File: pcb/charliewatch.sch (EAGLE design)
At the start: 85 parts, among them U2 CC430F5137IRGZR, X1 CRYSTALS-NOGND-IQXC-25, X2 FA-128

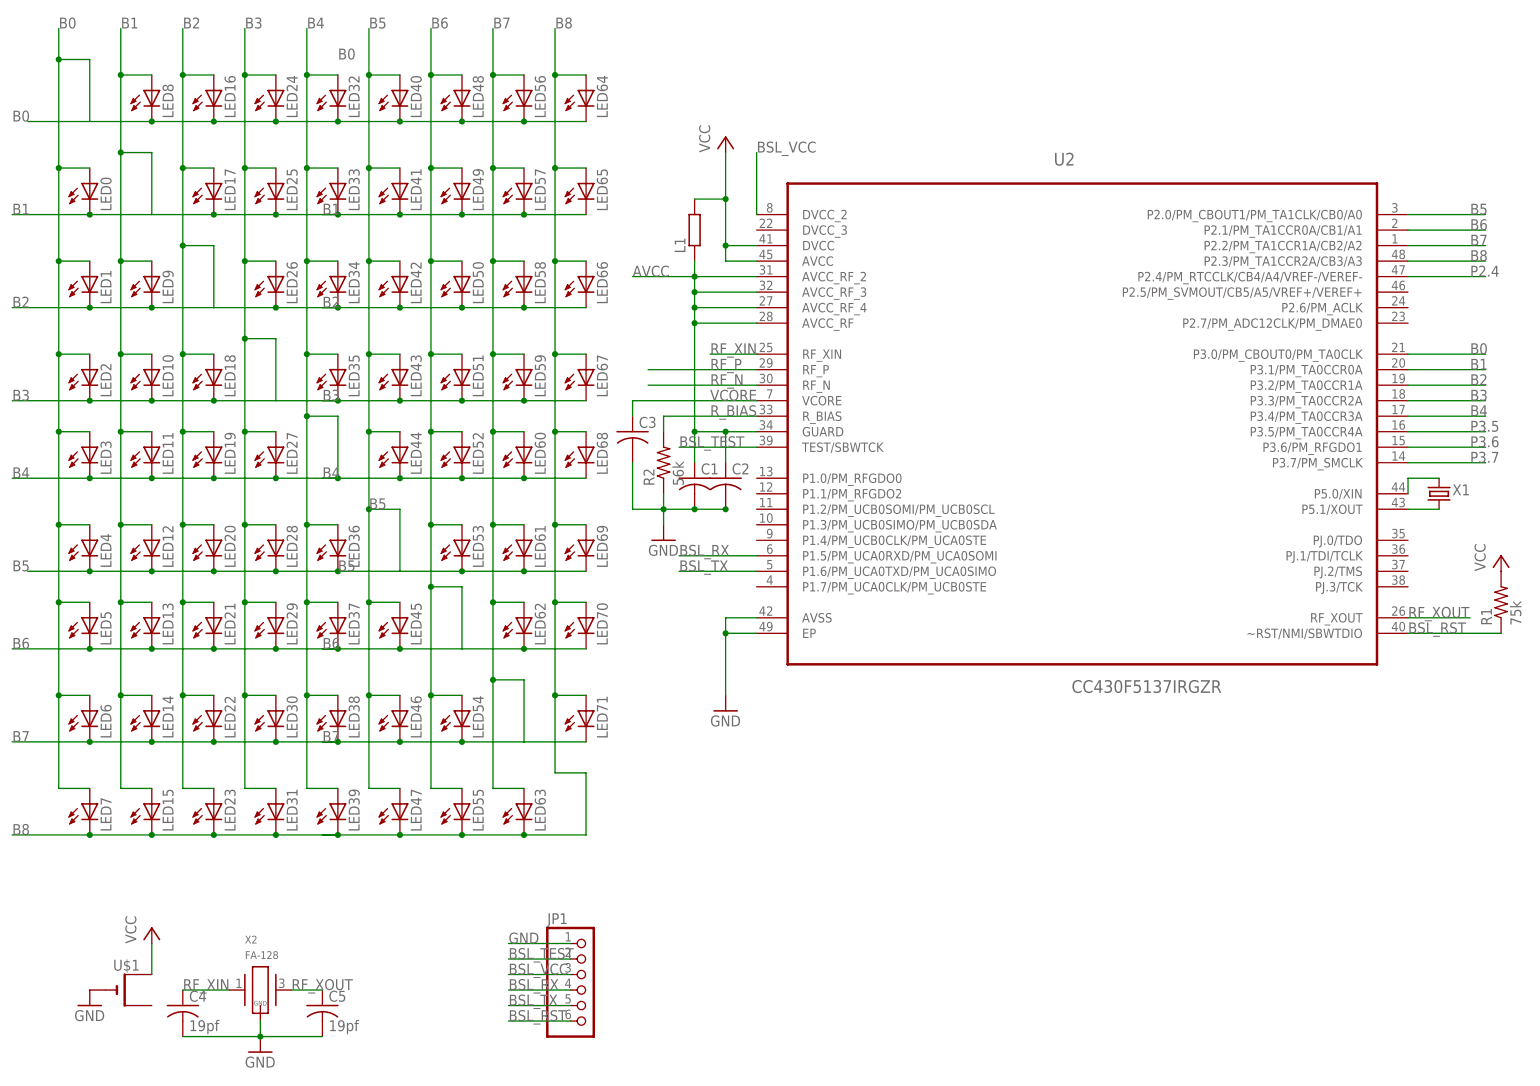
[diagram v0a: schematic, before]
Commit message: fixed drc errors, one missing vcc pin
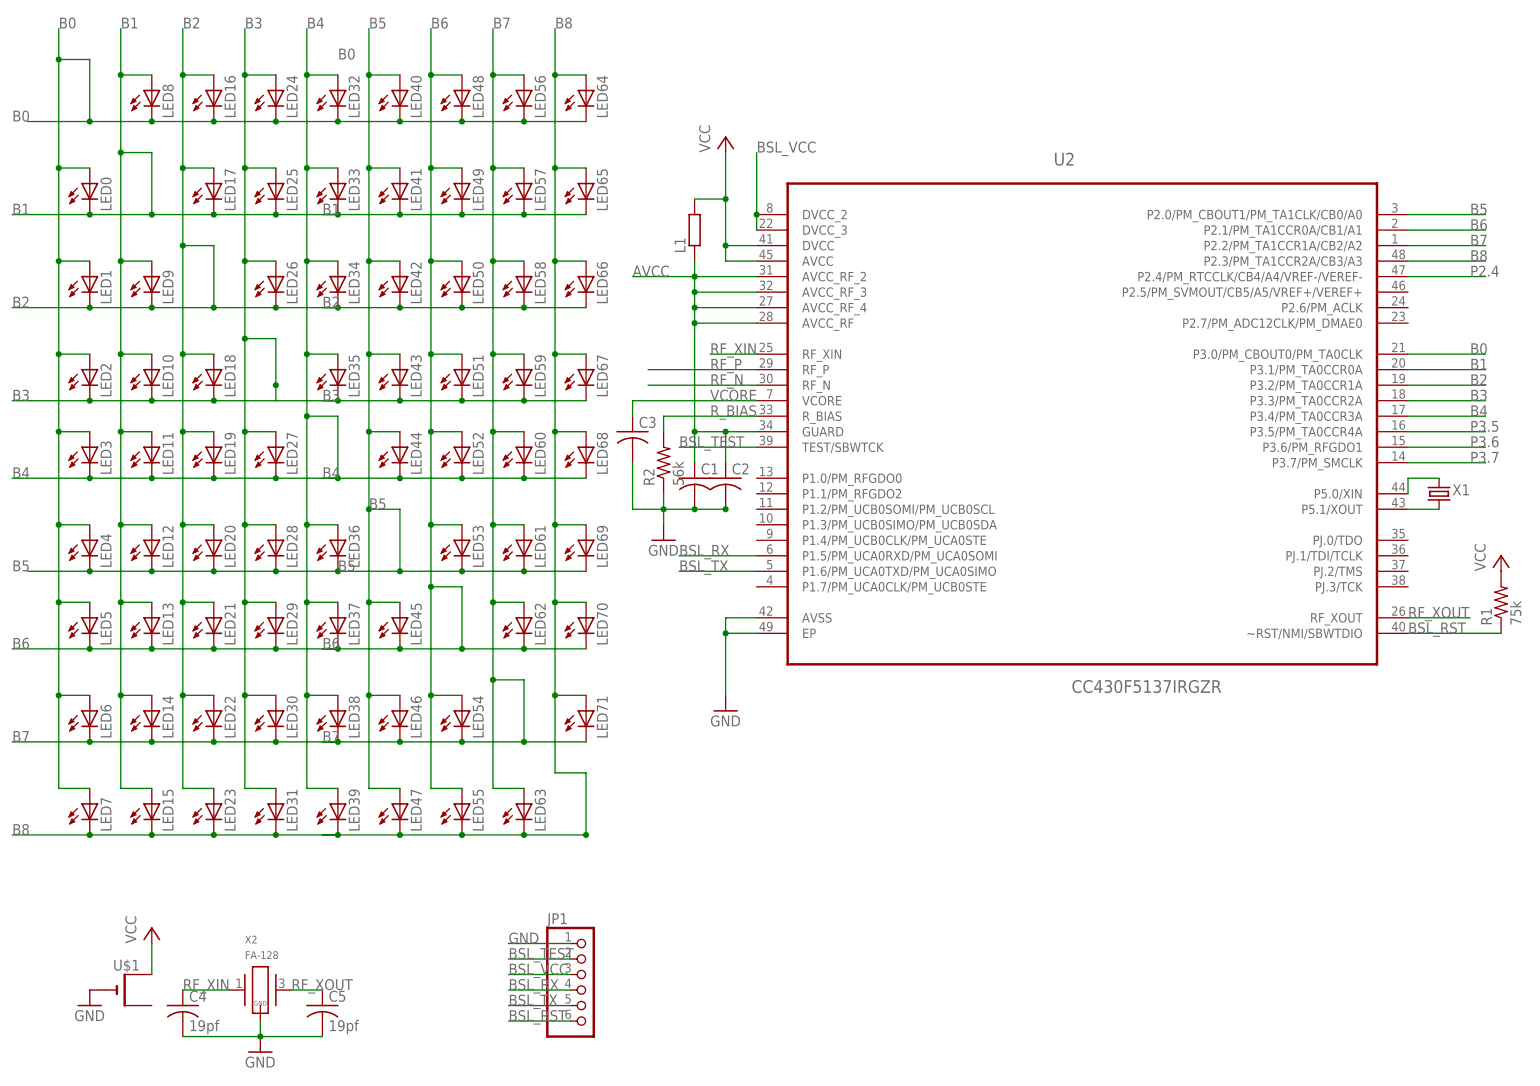
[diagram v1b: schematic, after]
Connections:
- net BSL_VCC: now also U2.DVCC_3
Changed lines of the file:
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@@
 <pinref part="LED67" gate="G$1" pin="C"/>
 <junction x="55.88" y="119.38"/>
-<wire x1="45.72" y1="129.54" x2="45.72" y2="119.38" width="0.1524" layer="91"/>
+<wire x1="45.72" y1="129.54" x2="45.72" y2="121.92" width="0.1524" layer="91"/>
+<junction x="45.72" y="121.92"/>
+<wire x1="45.72" y1="121.92" x2="45.72" y2="119.38" width="0.1524" layer="91"/>
 </segment>
 <segment>
@@
 <junction x="55.88" y="134.62"/>
 <wire x1="35.56" y1="144.78" x2="35.56" y2="134.62" width="0.1524" layer="91"/>
+<junction x="35.56" y="134.62"/>
 </segment>
 <segment>
@@
 <junction x="55.88" y="149.86"/>
 <wire x1="25.4" y1="160.02" x2="25.4" y2="149.86" width="0.1524" layer="91"/>
+<junction x="25.4" y="149.86"/>
 </segment>
 <segment>
@@
 <junction x="55.88" y="165.1"/>
 <wire x1="15.24" y1="175.26" x2="15.24" y2="165.1" width="0.1524" layer="91"/>
+<junction x="15.24" y="165.1"/>
 </segment>
 <segment>
@@
 <junction x="91.44" y="99.06"/>
 <wire x1="96.52" y1="48.26" x2="96.52" y2="58.42" width="0.1524" layer="91"/>
+<junction x="96.52" y="48.26"/>
 </segment>
 <segment>
@@
 <junction x="55.88" y="63.5"/>
 <wire x1="86.36" y1="73.66" x2="86.36" y2="63.5" width="0.1524" layer="91"/>
+<junction x="86.36" y="63.5"/>
 </segment>
 <segment>
@@
 <junction x="55.88" y="78.74"/>
 <wire x1="76.2" y1="88.9" x2="76.2" y2="78.74" width="0.1524" layer="91"/>
+<junction x="76.2" y="78.74"/>
 </segment>
 <segment>
@@
 <junction x="55.88" y="91.44"/>
 <wire x1="66.04" y1="101.6" x2="66.04" y2="91.44" width="0.1524" layer="91"/>
+<junction x="66.04" y="91.44"/>
 </segment>
 <segment>
@@
 <wire x1="124.46" y1="149.86" x2="124.46" y2="160.02" width="0.1524" layer="91"/>
 <label x="124.46" y="160.02" size="1.778" layer="95"/>
-</segment>
-<segment>
+<pinref part="U2" gate="A" pin="DVCC_3"/>
+<wire x1="124.46" y1="147.32" x2="124.46" y2="149.86" width="0.1524" layer="91"/>
+<junction x="124.46" y="149.86"/>
+</segment>
+<segment>

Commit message: replace with "1x6 lock" part
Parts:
- JP1: device adafruit:PINHD-1X6 -> adafruit:PINHD-1X6LOCK
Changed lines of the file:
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@@
 <grid distance="0.1" unitdist="inch" unit="inch" style="lines" multiple="1" display="no" altdistance="0.01" altunitdist="inch" altunit="inch"/>
 <layers>
-<layer number="1" name="Top" color="4" fill="1" visible="no" active="no"/>
-<layer number="2" name="Route2" color="1" fill="3" visible="no" active="no"/>
-<layer number="3" name="Route3" color="4" fill="3" visible="no" active="no"/>
-<layer number="14" name="Route14" color="1" fill="6" visible="no" active="no"/>
-<layer number="15" name="Route15" color="4" fill="6" visible="no" active="no"/>
-<layer number="16" name="Bottom" color="1" fill="1" visible="no" active="no"/>
-<layer number="17" name="Pads" color="2" fill="1" visible="no" active="no"/>
-<layer number="18" name="Vias" color="2" fill="1" visible="no" active="no"/>
-<layer number="19" name="Unrouted" color="6" fill="1" visible="no" active="no"/>
-<layer number="20" name="Dimension" color="15" fill="1" visible="no" active="no"/>
-<layer number="21" name="tPlace" color="7" fill="1" visible="no" active="no"/>
-<layer number="22" name="bPlace" color="7" fill="1" visible="no" active="no"/>
-<layer number="23" name="tOrigins" color="15" fill="1" visible="no" active="no"/>
-<layer number="24" name="bOrigins" color="15" fill="1" visible="no" active="no"/>
-<layer number="25" name="tNames" color="7" fill="1" visible="no" active="no"/>
-<layer number="26" name="bNames" color="7" fill="1" visible="no" active="no"/>
-<layer number="27" name="tValues" color="7" fill="1" visible="no" active="no"/>
-<layer number="28" name="bValues" color="7" fill="1" visible="no" active="no"/>
+<layer number="1" name="Top" color="4" fill="1" visible="yes" active="no"/>
+<layer number="2" name="Route2" color="1" fill="3" visible="yes" active="no"/>
+<layer number="3" name="Route3" color="4" fill="3" visible="yes" active="no"/>
+<layer number="14" name="Route14" color="1" fill="6" visible="yes" active="no"/>
+<layer number="15" name="Route15" color="4" fill="6" visible="yes" active="no"/>
+<layer number="16" name="Bottom" color="1" fill="1" visible="yes" active="no"/>
+<layer number="17" name="Pads" color="2" fill="1" visible="yes" active="no"/>
+<layer number="18" name="Vias" color="2" fill="1" visible="yes" active="no"/>
+<layer number="19" name="Unrouted" color="6" fill="1" visible="yes" active="no"/>
+<layer number="20" name="Dimension" color="15" fill="1" visible="yes" active="no"/>
+<layer number="21" name="tPlace" color="7" fill="1" visible="yes" active="no"/>
+<layer number="22" name="bPlace" color="7" fill="1" visible="yes" active="no"/>
+<layer number="23" name="tOrigins" color="15" fill="1" visible="yes" active="no"/>
+<layer number="24" name="bOrigins" color="15" fill="1" visible="yes" active="no"/>
+<layer number="25" name="tNames" color="7" fill="1" visible="yes" active="no"/>
+<layer number="26" name="bNames" color="7" fill="1" visible="yes" active="no"/>
+<layer number="27" name="tValues" color="7" fill="1" visible="yes" active="no"/>
+<layer number="28" name="bValues" color="7" fill="1" visible="yes" active="no"/>
 <layer number="29" name="tStop" color="7" fill="3" visible="no" active="no"/>
 <layer number="30" name="bStop" color="7" fill="6" visible="no" active="no"/>
@@
 <layer number="35" name="tGlue" color="7" fill="4" visible="no" active="no"/>
 <layer number="36" name="bGlue" color="7" fill="5" visible="no" active="no"/>
-<layer number="37" name="tTest" color="7" fill="1" visible="no" active="no"/>
-<layer number="38" name="bTest" color="7" fill="1" visible="no" active="no"/>
+<layer number="37" name="tTest" color="7" fill="1" visible="yes" active="no"/>
+<layer number="38" name="bTest" color="7" fill="1" visible="yes" active="no"/>
 <layer number="39" name="tKeepout" color="4" fill="11" visible="no" active="no"/>
 <layer number="40" name="bKeepout" color="1" fill="11" visible="no" active="no"/>
@@
 <layer number="44" name="Drills" color="7" fill="1" visible="no" active="no"/>
 <layer number="45" name="Holes" color="7" fill="1" visible="no" active="no"/>
-<layer number="46" name="Milling" color="3" fill="1" visible="no" active="no"/>
-<layer number="47" name="Measures" color="7" fill="1" visible="no" active="no"/>
-<layer number="48" name="Document" color="7" fill="1" visible="no" active="no"/>
-<layer number="49" name="Reference" color="7" fill="1" visible="no" active="no"/>
-<layer number="50" name="dxf" color="7" fill="1" visible="no" active="no"/>
-<layer number="51" name="tDocu" color="7" fill="1" visible="no" active="no"/>
-<layer number="52" name="bDocu" color="7" fill="1" visible="no" active="no"/>
-<layer number="53" name="tPadExt" color="7" fill="1" visible="no" active="no"/>
-<layer number="54" name="bPadExt" color="1" fill="1" visible="no" active="no"/>
-<layer number="56" name="wert" color="7" fill="1" visible="no" active="no"/>
-<layer number="57" name="tCAD" color="7" fill="1" visible="no" active="no"/>
-<layer number="59" name="tCarbon" color="7" fill="1" visible="no" active="no"/>
-<layer number="60" name="bCarbon" color="7" fill="1" visible="no" active="no"/>
+<layer number="46" name="Milling" color="3" fill="1" visible="yes" active="no"/>
+<layer number="47" name="Measures" color="7" fill="1" visible="yes" active="no"/>
+<layer number="48" name="Document" color="7" fill="1" visible="yes" active="no"/>
+<layer number="49" name="Reference" color="7" fill="1" visible="yes" active="no"/>
+<layer number="50" name="dxf" color="7" fill="1" visible="yes" active="no"/>
+<layer number="51" name="tDocu" color="7" fill="1" visible="yes" active="no"/>
+<layer number="52" name="bDocu" color="7" fill="1" visible="yes" active="no"/>
+<layer number="53" name="tPadExt" color="7" fill="1" visible="yes" active="no"/>
+<layer number="54" name="bPadExt" color="1" fill="1" visible="yes" active="no"/>
+<layer number="56" name="wert" color="7" fill="1" visible="yes" active="no"/>
+<layer number="57" name="tCAD" color="7" fill="1" visible="yes" active="no"/>
+<layer number="59" name="tCarbon" color="7" fill="1" visible="yes" active="no"/>
+<layer number="60" name="bCarbon" color="7" fill="1" visible="yes" active="no"/>
 <layer number="90" name="Modules" color="5" fill="1" visible="yes" active="yes"/>
 <layer number="91" name="Nets" color="2" fill="1" visible="yes" active="yes"/>
@@
 <part name="C5" library="resistor" deviceset="C-US" device="C0603" value="19pf"/>
 <part name="U$1" library="adafruit" deviceset="CR2032" device="SMT"/>
-<part name="JP1" library="adafruit" deviceset="PINHD-1X6" device=""/>
+<part name="JP1" library="adafruit" deviceset="PINHD-1X6" device="LOCK"/>
 </parts>
 <sheets>
